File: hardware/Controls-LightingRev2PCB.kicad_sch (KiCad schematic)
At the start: 37 parts, among them IC2 AP2205-W5-7, IC3 ACS724LLCTR-05AU-T, IC4 ACS724LLCTR-05AU-T, IC6 ACS724LLCTR-05AU-T, J1 53307-2471, J3 Conn_02x05_Top_Bottom, J4 Conn_01x02, J5 Conn_01x02, J6 Conn_01x03, Q3 IRLML0030, Q5 IRLML0030, U5 SN74LV1T34DBV

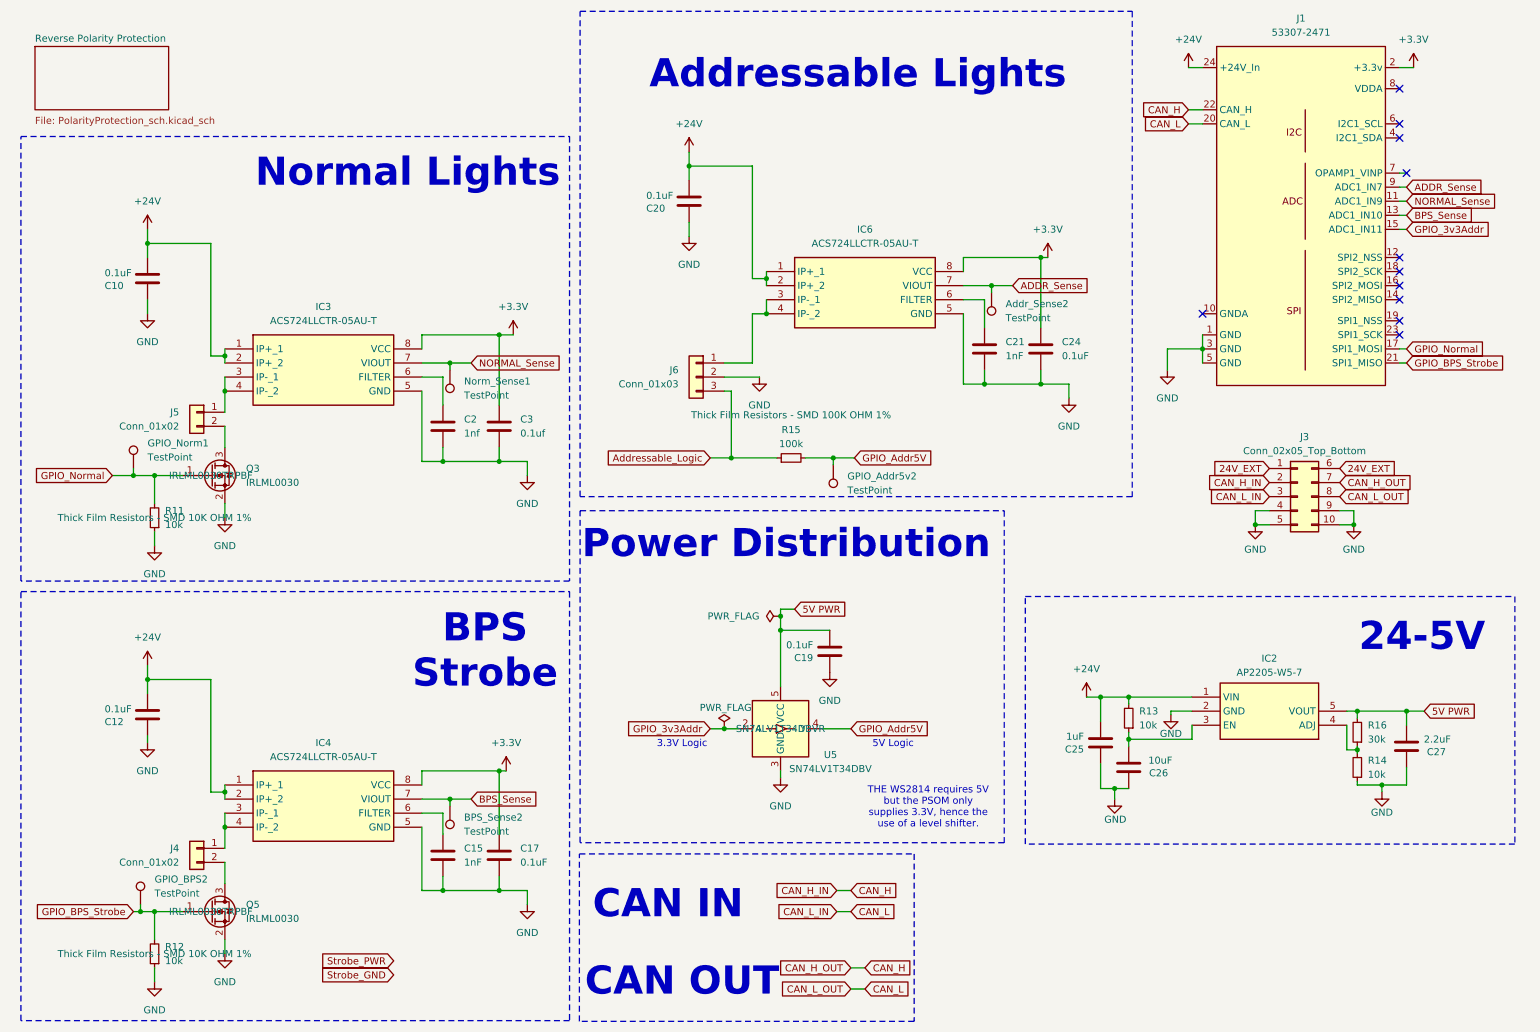
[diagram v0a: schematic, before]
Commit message: Layout with 0 DRS and polarity errors
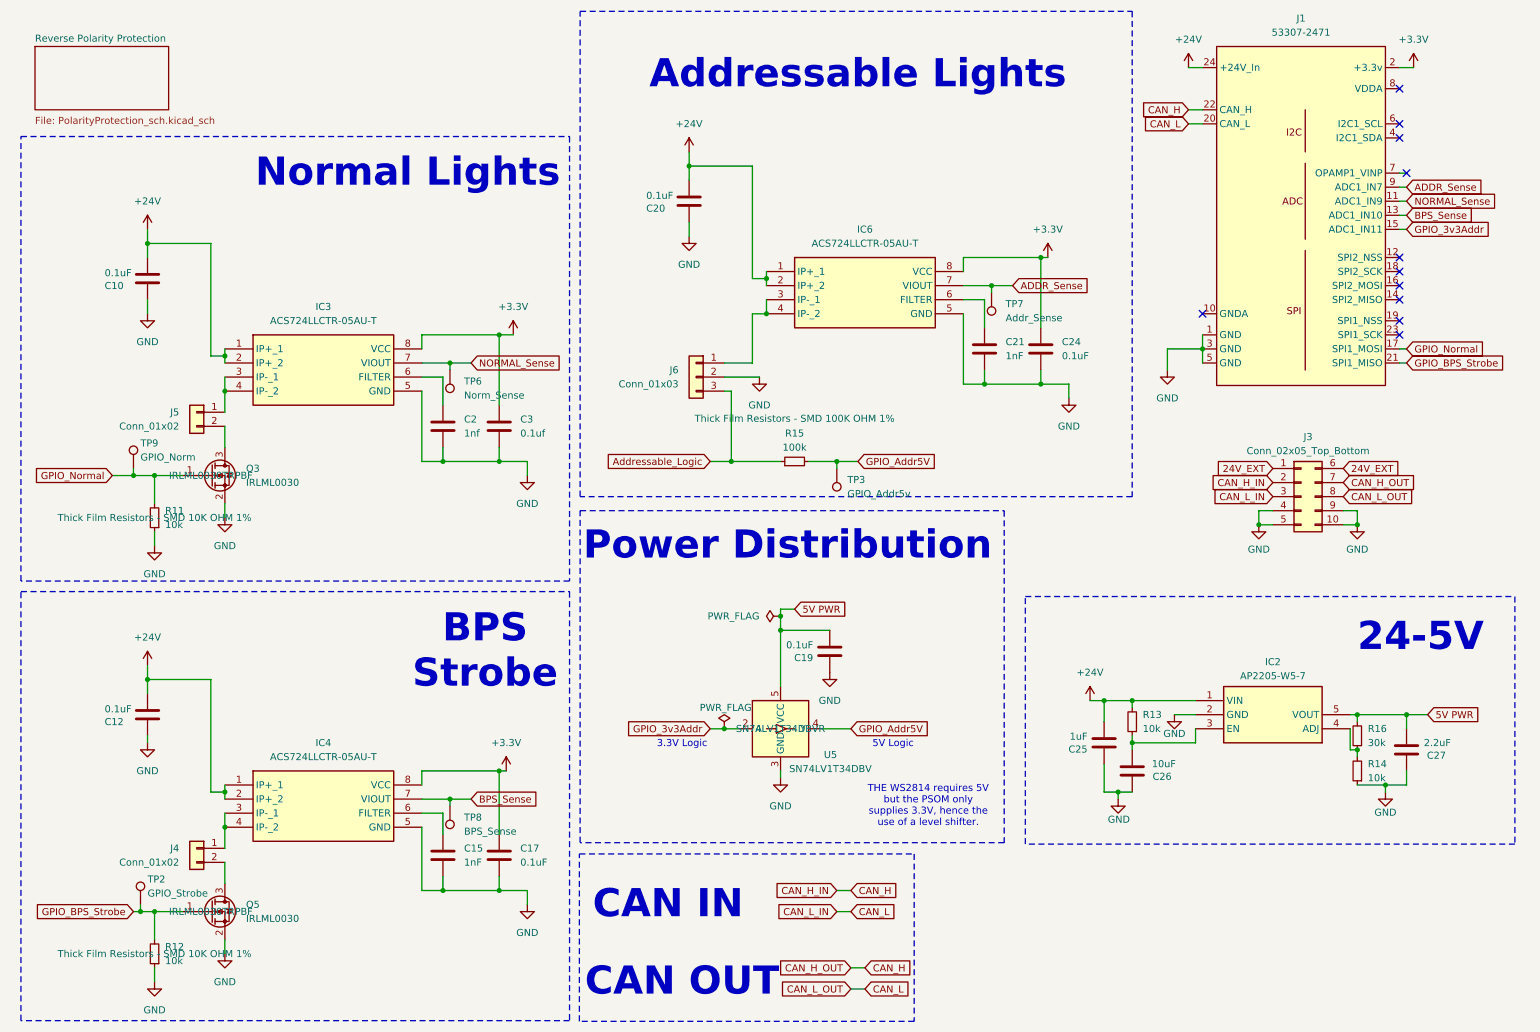
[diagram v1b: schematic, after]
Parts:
- removed Addr_Sense2, BPS_Sense2, GPIO_Addr5v2, GPIO_BPS2, GPIO_Norm1, Norm_Sense1: TestPoint, TestPoint:TestPoint_Keystone_5005-5009_Compact, symbol Connector:TestPoint
- added TP2: GPIO_Strobe, TestPoint:TestPoint_Keystone_5005-5009_Compact, symbol Connector:TestPoint
- added TP3: GPIO_Addr5v, TestPoint:TestPoint_Keystone_5005-5009_Compact, symbol Connector:TestPoint
- added TP6: Norm_Sense, TestPoint:TestPoint_Keystone_5005-5009_Compact, symbol Connector:TestPoint
- added TP7: Addr_Sense, TestPoint:TestPoint_Keystone_5005-5009_Compact, symbol Connector:TestPoint
- added TP8: BPS_Sense, TestPoint:TestPoint_Keystone_5005-5009_Compact, symbol Connector:TestPoint
- added TP9: GPIO_Norm, TestPoint:TestPoint_Keystone_5005-5009_Compact, symbol Connector:TestPoint
- IC2: footprint AP2205W57 -> LDO:AP2205W57
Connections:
- net ADDR_Sense: now also TP7.1
- net BPS_Sense: now also TP8.1
- net GPIO_Addr5V: now also TP3.1
- net GPIO_BPS_Strobe: now also TP2.1
- net GPIO_Normal: now also TP9.1
- net NORMAL_Sense: now also TP6.1
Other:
- moved on the sheet: C25, C26, C27, IC2, J3, R13, R14, R15, R16

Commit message: Bom and Final Layout
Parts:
- C15, C21: P/N (none) -> MLASU063SB7102KFNA01
- C17, C24: P/N (none) -> MLASH168SB7104KTNA01
- C2: value 1nf -> 1nF; P/N (none) -> MLASU063SB7102KFNA01
- C26: P/N MLASH168SB7104KTNA01 -> GRM21BR61H106KE43K
- C27: P/N MLASH168SB7104KTNA01 -> GRT188R61H225KE13D
- C3: value 0.1uf -> 0.1uF; P/N (none) -> MLASH168SB7104KTNA01
- IC2: P/N (none) -> AP2205-W5-7
- IC3, IC4, IC6: P/N (none) -> ACS724LLCTR-05AU-T
- J3: P/N (none) -> 1053141310
- J4, J5: P/N (none) -> 1053132102
- J6: P/N (none) -> 1053131103
- R16: P/N CRCW060310K0FKEI -> CRCW060330K0FKEA
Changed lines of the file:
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@@
 			)
 		)
+		(property "P/N" "ACS724LLCTR-05AU-T"
+			(at 50.8 74.93 0)
+			(effects
+				(font
+					(size 1.27 1.27)
+				)
+			)
+		)
 		(pin "4"
 		)
@@
 			)
 		)
+		(property "P/N" "ACS724LLCTR-05AU-T"
+			(at 148.59 60.96 0)
+			(effects
+				(font
+					(size 1.27 1.27)
+				)
+			)
+		)
 		(pin "4"
 		)
@@
 			)
 		)
+		(property "P/N" "AP2205-W5-7 "
+			(at 254 143.51 0)
+			(effects
+				(font
+					(size 1.27 1.27)
+				)
+			)
+		)
 		(pin "5"
 		)
@@
 			)
 		)
+		(property "P/N" "1053132102"
+			(at 45.72 165.1 0)
+			(effects
+				(font
+					(size 1.27 1.27)
+				)
+			)
+		)
 		(pin "1"
 		)
@@
 			)
 		)
+		(property "P/N" "MLASU063SB7102KFNA01"
+			(at 90.17 166.37 0)
+			(effects
+				(font
+					(size 1.27 1.27)
+				)
+			)
+		)
 		(pin "2"
 		)
@@
 			)
 		)
-		(property "P/N" "MLASH168SB7104KTNA01"
+		(property "P/N" "GRM21BR61H106KE43K"
 			(at 214.63 151.13 0)
 			(effects
@@
 			)
 		)
+		(property "P/N" "MLASH168SB7104KTNA01"
+			(at 198.12 74.93 0)
+			(effects
+				(font
+					(size 1.27 1.27)
+				)
+			)
+		)
 		(pin "2"
 		)
@@
 			)
 		)
+		(property "P/N" "MLASU063SB7102KFNA01"
+			(at 187.96 74.93 0)
+			(effects
+				(font
+					(size 1.27 1.27)
+				)
+			)
+		)
 		(pin "2"
 		)
@@
 			)
 		)
-		(property "Value" "1nf"
+		(property "Value" "1nF"
 			(at 93.98 90.1699 0)
 			(effects
@@
 			)
 		)
+		(property "P/N" "MLASU063SB7102KFNA01"
+			(at 90.17 88.9 0)
+			(effects
+				(font
+					(size 1.27 1.27)
+				)
+			)
+		)
 		(pin "2"
 		)
@@
 			)
 		)
-		(property "P/N" "CRCW060310K0FKEI "
+		(property "P/N" "CRCW060330K0FKEA"
 			(at 255.27 144.78 0)
 			(effects
@@
 			)
 		)
+		(property "P/N" "MLASH168SB7104KTNA01"
+			(at 100.33 166.37 0)
+			(effects
+				(font
+					(size 1.27 1.27)
+				)
+			)
+		)
 		(pin "2"
 		)
@@
 			)
 		)
+		(property "P/N" "1053141310"
+			(at 245.11 101.6 0)
+			(effects
+				(font
+					(size 1.27 1.27)
+				)
+			)
+		)
 		(pin "2"
 		)
@@
 			)
 		)
-		(property "Value" "0.1uf"
+		(property "Value" "0.1uF"
 			(at 104.14 90.1699 0)
 			(effects
@@
 			)
 		)
+		(property "P/N" "MLASH168SB7104KTNA01"
+			(at 100.33 88.9 0)
+			(effects
+				(font
+					(size 1.27 1.27)
+				)
+			)
+		)
 		(pin "2"
 		)
@@
 			)
 		)
+		(property "P/N" "ACS724LLCTR-05AU-T"
+			(at 50.8 153.67 0)
+			(effects
+				(font
+					(size 1.27 1.27)
+				)
+			)
+		)
 		(pin "4"
 		)
@@
 			)
 		)
-		(property "P/N" "MLASH168SB7104KTNA01"
+		(property "P/N" "GRT188R61H225KE13D"
 			(at 264.16 147.32 0)
 			(effects
@@
 			)
 		)
+		(property "P/N" "1053131103 "
+			(at 135.89 80.01 0)
+			(effects
+				(font
+					(size 1.27 1.27)
+				)
+			)
+		)
 		(pin "1"
 		)
@@
 			)
 		)
+		(property "P/N" "1053132102"
+			(at 45.72 86.36 0)
+			(effects
+				(font
+					(size 1.27 1.27)
+				)
+			)
+		)

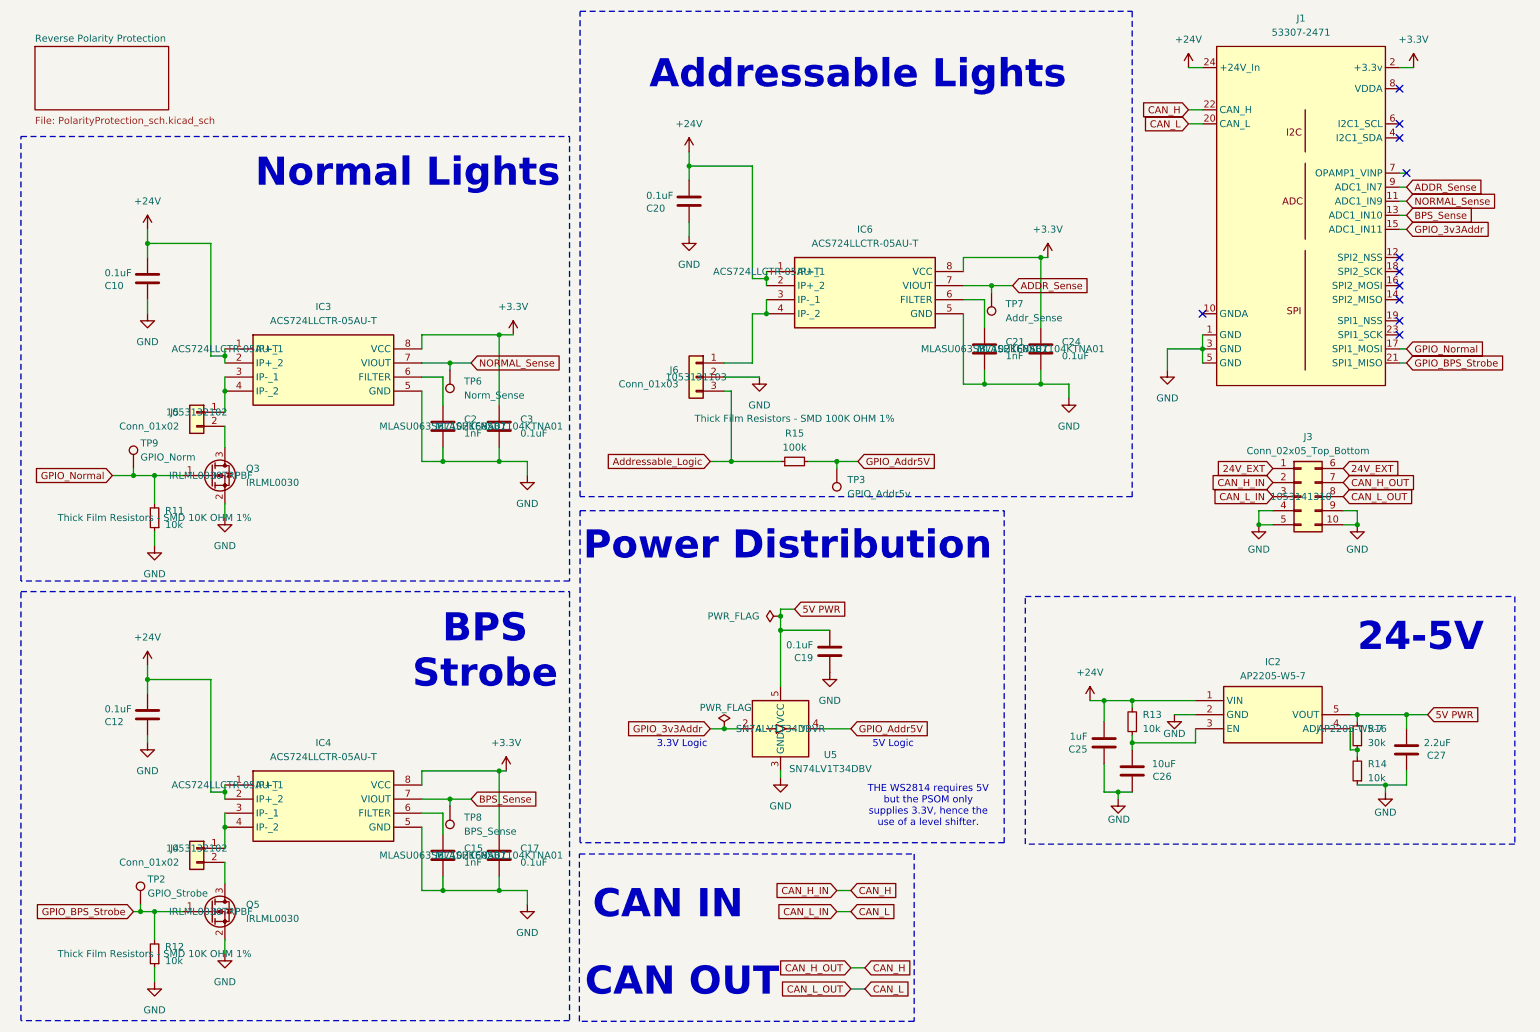
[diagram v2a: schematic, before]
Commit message: add JLCPCB assembly files
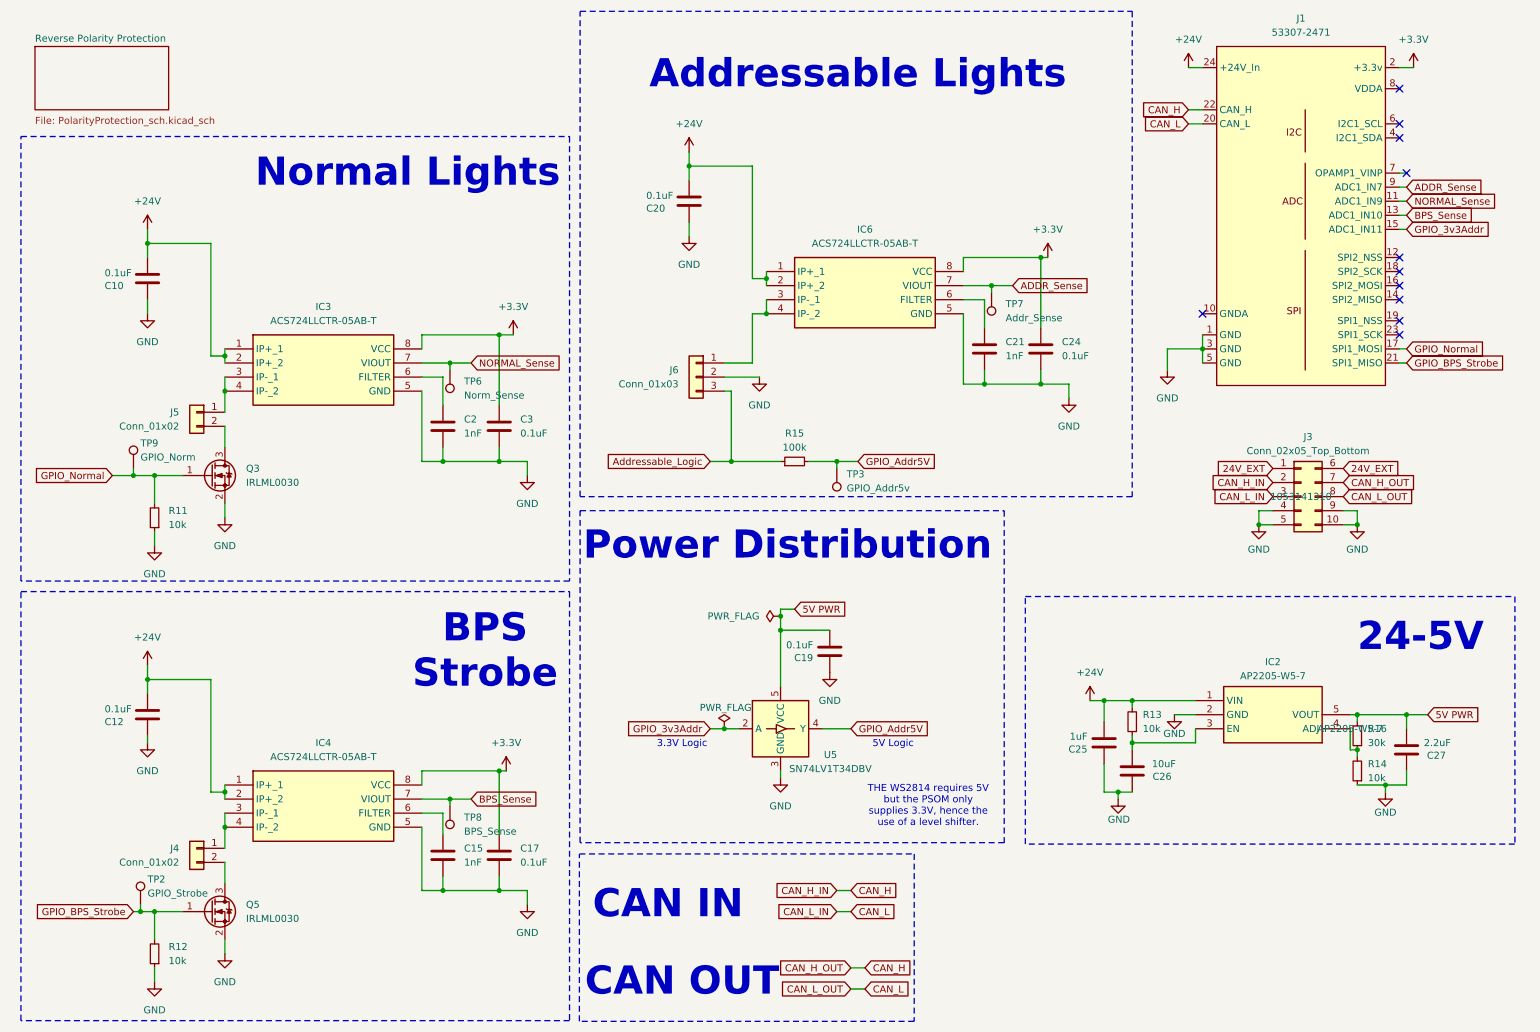
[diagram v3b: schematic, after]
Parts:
- C10, C12, C17, C19, C20, C24, C3: LCSC P/N (none) -> C14663
- C15, C2, C21: LCSC P/N (none) -> C1588
- C25: LCSC P/N (none) -> C15849
- C26: footprint Capacitor_SMD:C_0603_1608Metric -> Capacitor_SMD:C_0805_2012Metric_Pad1.18x1.45mm_HandSolder; LCSC P/N (none) -> C440198
- C27: LCSC P/N (none) -> C57895
- IC2: LCSC P/N (none) -> C3001658
- IC3: value ACS724LLCTR-05AU-T -> ACS724LLCTR-05AB-T; LCSC P/N (none) -> C22392329; Manufacturer_Part_Number ACS724LLCTR-05AU-T -> (none); Mouser Part Number 250-724LLCTR05AUT -> (none); Mouser Price/Stock https://www.mouser.co.uk/ProductDetail/Allegro-MicroSystems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 -> (none); P/N ACS724LLCTR-05AU-T -> ACS724LLCTR-05AB-T
- IC4: value ACS724LLCTR-05AU-T -> ACS724LLCTR-05AB-T; LCSC P/N (none) -> C22392329; Manufacturer_Name Allegro Microsystems -> (none); Manufacturer_Part_Number ACS724LLCTR-05AU-T -> ACS724LLCTR-05AB-T; Mouser Part Number 250-724LLCTR05AUT -> (none); Mouser Price/Stock https://www.mouser.co.uk/ProductDetail/Allegro-MicroSystems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 -> (none); P/N ACS724LLCTR-05AU-T -> ACS724LLCTR-05AB-T
- IC6: value ACS724LLCTR-05AU-T -> ACS724LLCTR-05AB-T; LCSC P/N (none) -> C22392329; Manufacturer_Part_Number ACS724LLCTR-05AU-T -> ACS724LLCTR-05AB-T; Mouser Part Number 250-724LLCTR05AUT -> ACS724LLCTR-05AB-T; P/N ACS724LLCTR-05AU-T -> ACS724LLCTR-05AB-T
- Q3, Q5: LCSC P/N (none) -> C67272
- R11, R12, R13, R14: LCSC P/N (none) -> C25804
- R15: LCSC P/N (none) -> C25803
- R16: LCSC P/N (none) -> C18681
- U5: LCSC P/N (none) -> C47117565
